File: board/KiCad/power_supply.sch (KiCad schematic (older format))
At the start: 6 parts, among them CON1 BARREL_JACK, Q1 IRLML6344bpf

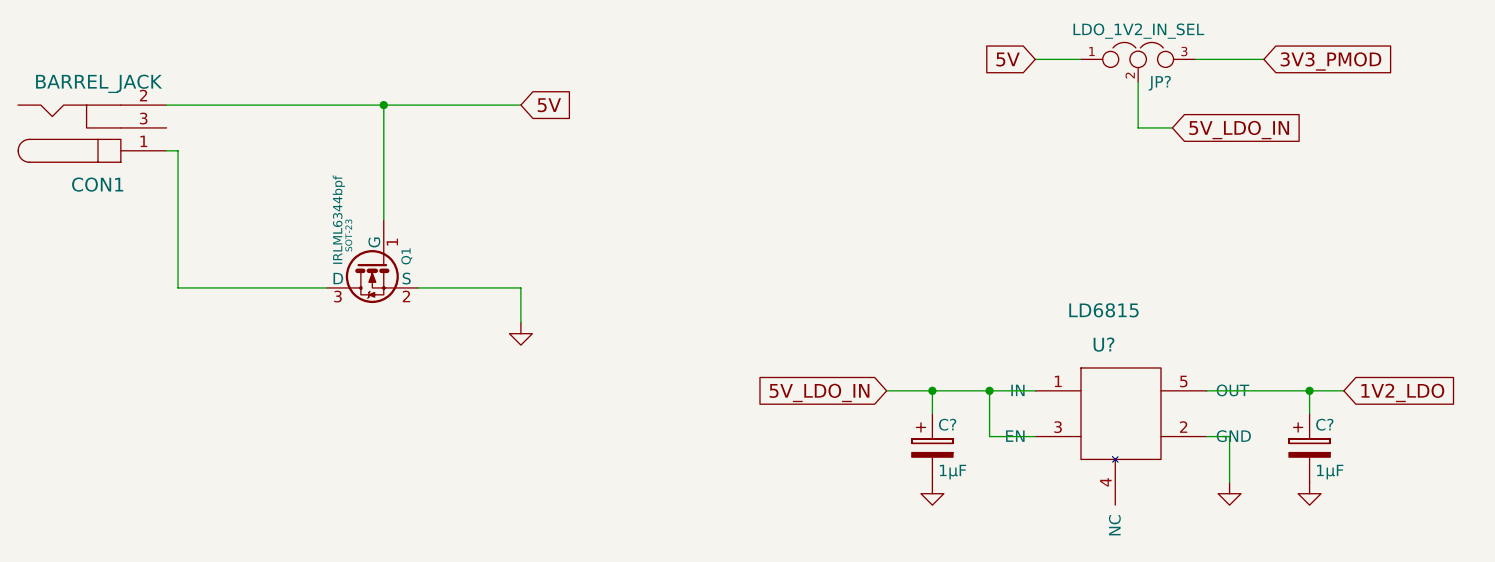
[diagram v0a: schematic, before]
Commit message: added overcurrent/voltage protection
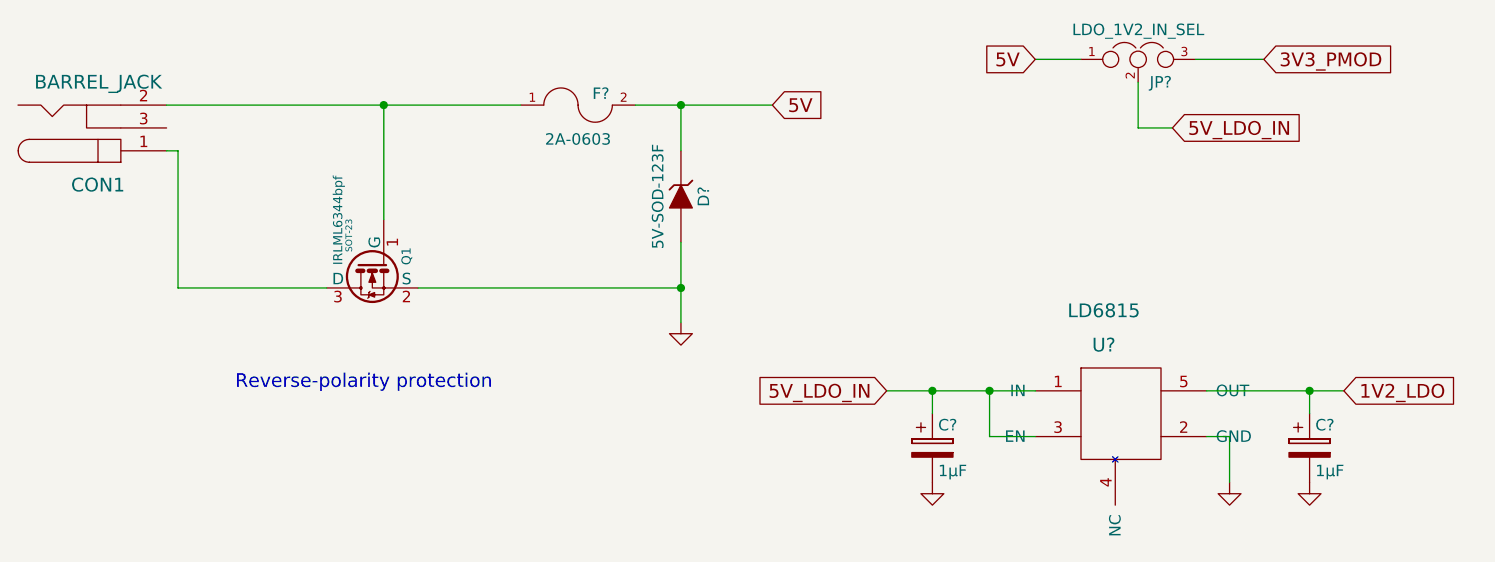
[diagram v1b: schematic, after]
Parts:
- added D?: 5V-SOD-123F, symbol ZENER
- added F?: 2A-0603, symbol FUSE
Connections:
- wire segments 19 -> 21
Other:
- note added: "Reverse-polarity protection"
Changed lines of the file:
@@
 EESchema Schematic File Version 2
-LIBS:LMS6002-Pmod-rescue
 LIBS:power
 LIBS:device
@@
 	2400 2500 3050 2500
 Wire Wire Line
-	3450 2500 3900 2500
+	3450 2500 4600 2500
 Connection ~ 3300 1700
 $Comp
 L GND #PWR6
 U 1 1 56A748C9
-P 3900 2650
-F 0 "#PWR6" H 3900 2650 30  0001 C CNN
-F 1 "GND" H 3900 2580 30  0001 C CNN
-F 2 "" H 3900 2650 60  0000 C CNN
-F 3 "" H 3900 2650 60  0000 C CNN
-	1    3900 2650
-	1    0    0    -1
-$EndComp
-Wire Wire Line
-	3900 2500 3900 2650
-Text GLabel 3900 1700 2    60   Input ~ 0
+P 4600 2650
+F 0 "#PWR6" H 4600 2650 30  0001 C CNN
+F 1 "GND" H 4600 2580 30  0001 C CNN
+F 2 "" H 4600 2650 60  0000 C CNN
+F 3 "" H 4600 2650 60  0000 C CNN
+	1    4600 2650
+	1    0    0    -1
+$EndComp
+Text GLabel 5000 1700 2    60   Input ~ 0
 5V
 $Comp
@@
 	1    0    0    -1
 $EndComp
+Text Notes 2650 2950 0    60   ~ 0
+Reverse-polarity protection
+$Comp
+L FUSE F?
+U 1 1 56AB7E87
+P 4150 1700
+F 0 "F?" H 4250 1750 50  0000 C CNN
+F 1 "2A-0603" H 4150 1550 50  0000 C CNN
+F 2 "" H 4150 1700 50  0000 C CNN
+F 3 "" H 4150 1700 50  0000 C CNN
+	1    4150 1700
+	1    0    0    -1
+$EndComp
+$Comp
+L ZENER D?
+U 1 1 56AB7F42
+P 4600 2100
+F 0 "D?" H 4600 2200 50  0000 C CNN
+F 1 "5V-SOD-123F" H 4600 2000 50  0000 C CNN
+F 2 "" H 4600 2100 50  0000 C CNN
+F 3 "" H 4600 2100 50  0000 C CNN
+	1    4600 2100
+	0    1    1    0
+$EndComp
+Wire Wire Line
+	4400 1700 5000 1700
+Wire Wire Line
+	4600 1900 4600 1700
+Connection ~ 4600 1700
+Wire Wire Line
+	4600 2300 4600 2650
+Connection ~ 4600 2500
 $EndSCHEMATC

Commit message: removed legacy footprints
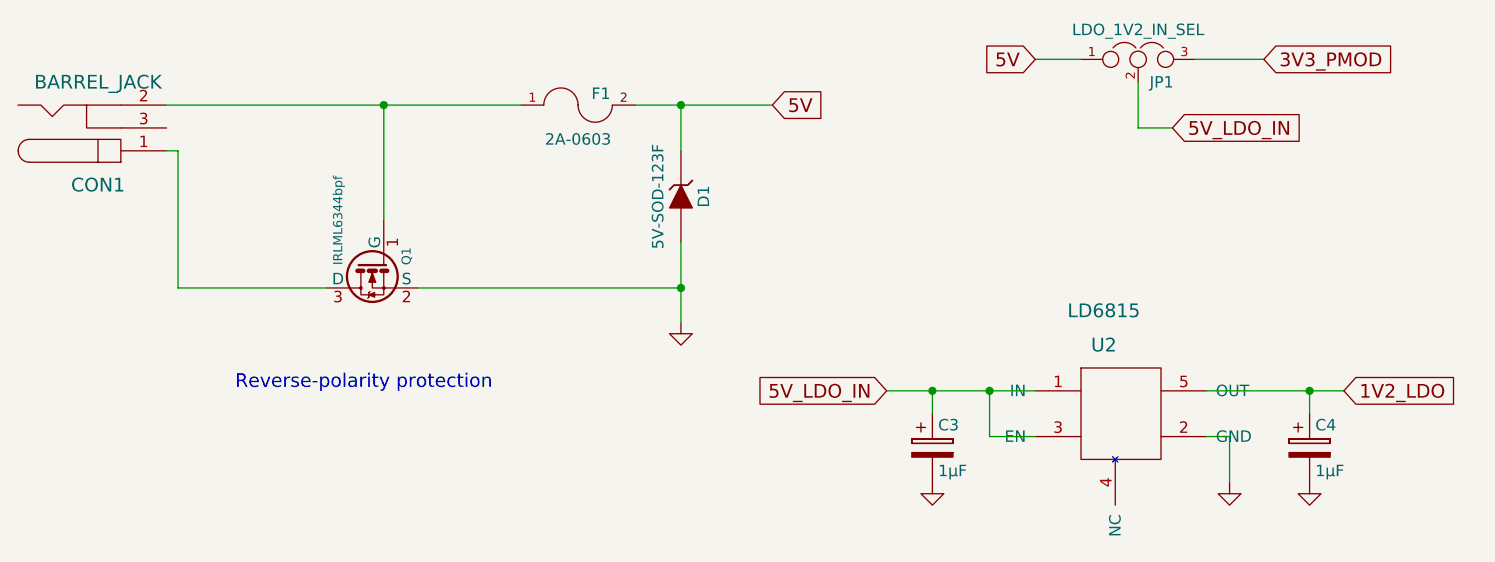
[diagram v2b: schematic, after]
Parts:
- Q1: footprint SOT-23 -> (none)
- gave numbers to parts that had none: 6
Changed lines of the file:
@@
 F 0 "Q1" H 3250 2251 40  0000 R CNN
 F 1 "IRLML6344bpf" H 3250 2550 40  0000 R CNN
-F 2 "SOT-23" H 3120 2502 29  0000 C CNN
+F 2 "" H 3120 2502 29  0000 C CNN
 F 3 "" H 3250 2400 60  0000 C CNN
 	1    3250 2400
@@
 Connection ~ 3300 1700
 $Comp
-L GND #PWR6
+L GND #PWR14
 U 1 1 56A748C9
 P 4600 2650
-F 0 "#PWR6" H 4600 2650 30  0001 C CNN
+F 0 "#PWR14" H 4600 2650 30  0001 C CNN
 F 1 "GND" H 4600 2580 30  0001 C CNN
 F 2 "" H 4600 2650 60  0000 C CNN
@@
 F 0 "CON1" H 2050 2050 60  0000 C CNN
 F 1 "BARREL_JACK" H 2050 1600 60  0000 C CNN
-F 2 "" H 2050 1800 60  0000 C CNN
+F 2 "" H 2050 1800 60  0001 C CNN
 F 3 "" H 2050 1800 60  0000 C CNN
 	1    2050 1800
@@
 $EndComp
 $Comp
-L LD6815 U?
+L LD6815 U2
 U 1 1 56AB720B
 P 6450 2750
-F 0 "U?" H 6450 2750 60  0000 C CNN
+F 0 "U2" H 6450 2750 60  0000 C CNN
 F 1 "LD6815" H 6450 2900 60  0000 C CNN
-F 2 "" H 6450 2750 60  0000 C CNN
+F 2 "" H 6450 2750 60  0001 C CNN
 F 3 "" H 6450 2750 60  0000 C CNN
 	1    6450 2750
@@
 	6900 2950 7500 2950
 $Comp
-L GND #PWR?
+L GND #PWR16
 U 1 1 56AB761D
 P 7000 3350
-F 0 "#PWR?" H 7000 3350 30  0001 C CNN
+F 0 "#PWR16" H 7000 3350 30  0001 C CNN
 F 1 "GND" H 7000 3280 30  0001 C CNN
 F 2 "" H 7000 3350 60  0000 C CNN
@@
 1V2_LDO
 $Comp
-L JUMPER3 JP?
+L JUMPER3 JP1
 U 1 1 56AB7982
 P 6600 1500
-F 0 "JP?" H 6650 1400 50  0000 L CNN
+F 0 "JP1" H 6650 1400 50  0000 L CNN
 F 1 "LDO_1V2_IN_SEL" H 6600 1600 50  0000 C BNN
-F 2 "" H 6600 1500 60  0000 C CNN
+F 2 "" H 6600 1500 60  0001 C CNN
 F 3 "" H 6600 1500 60  0000 C CNN
 	1    6600 1500
@@
 	6600 1800 6750 1800
 $Comp
-L CP C?
+L CP C4
 U 1 1 56AB817A
 P 7350 3200
-F 0 "C?" H 7375 3300 50  0000 L CNN
+F 0 "C4" H 7375 3300 50  0000 L CNN
 F 1 "1µF" H 7375 3100 50  0000 L CNN
-F 2 "" H 7388 3050 30  0000 C CNN
+F 2 "" H 7388 3050 30  0001 C CNN
 F 3 "" H 7350 3200 60  0000 C CNN
 	1    7350 3200
@@
 $EndComp
 $Comp
-L CP C?
+L CP C3
 U 1 1 56AB81CD
 P 5700 3200
-F 0 "C?" H 5725 3300 50  0000 L CNN
+F 0 "C3" H 5725 3300 50  0000 L CNN
 F 1 "1µF" H 5725 3100 50  0000 L CNN
-F 2 "" H 5738 3050 30  0000 C CNN
+F 2 "" H 5738 3050 30  0001 C CNN
 F 3 "" H 5700 3200 60  0000 C CNN
 	1    5700 3200
@@
 Connection ~ 7350 2950
 $Comp
-L GND #PWR?
+L GND #PWR17
 U 1 1 56AB861C
 P 7350 3350
-F 0 "#PWR?" H 7350 3350 30  0001 C CNN
+F 0 "#PWR17" H 7350 3350 30  0001 C CNN
 F 1 "GND" H 7350 3280 30  0001 C CNN
 F 2 "" H 7350 3350 60  0000 C CNN
@@
 $EndComp
 $Comp
-L GND #PWR?
+L GND #PWR15
 U 1 1 56AB8639
 P 5700 3350
-F 0 "#PWR?" H 5700 3350 30  0001 C CNN
+F 0 "#PWR15" H 5700 3350 30  0001 C CNN
 F 1 "GND" H 5700 3280 30  0001 C CNN
 F 2 "" H 5700 3350 60  0000 C CNN
@@
 Reverse-polarity protection
 $Comp
-L FUSE F?
+L FUSE F1
 U 1 1 56AB7E87
 P 4150 1700
-F 0 "F?" H 4250 1750 50  0000 C CNN
+F 0 "F1" H 4250 1750 50  0000 C CNN
 F 1 "2A-0603" H 4150 1550 50  0000 C CNN
-F 2 "" H 4150 1700 50  0000 C CNN
+F 2 "" H 4150 1700 50  0001 C CNN
 F 3 "" H 4150 1700 50  0000 C CNN
 	1    4150 1700
@@
 $EndComp
 $Comp
-L ZENER D?
+L ZENER D1
 U 1 1 56AB7F42
 P 4600 2100
-F 0 "D?" H 4600 2200 50  0000 C CNN
+F 0 "D1" H 4600 2200 50  0000 C CNN
 F 1 "5V-SOD-123F" H 4600 2000 50  0000 C CNN
-F 2 "" H 4600 2100 50  0000 C CNN
+F 2 "" H 4600 2100 50  0001 C CNN
 F 3 "" H 4600 2100 50  0000 C CNN
 	1    4600 2100
